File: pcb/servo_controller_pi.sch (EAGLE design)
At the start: 126 parts, among them IC1 PIC18F452, IC2 DS1307, IC3 MAX4173FESA+, IC4 LM2936MP-3.3, IC6 LM386M-1, IC7 GY-27, IC8 MCP23017SO, Q1 10Mhz, Q2 BC848ASMD, Q3 BC848ASMD

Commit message: BleuettePi encore !
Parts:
- removed D4, D5, D7: 5V1, diode:ZENER-DIODESOT23
- removed R19, R20, R21, R22: 10k, rcl:R-EU_M0805
- removed U$1: MCP3424-E/ST, eagleParts_MCP3424:MCP3424-E/ST
- added R30, R32, R34, R36: 10k 1%, rcl:R-EU_M0805
- added R31, R33, R35, R37: 6.8k 1%, rcl:R-EU_M0805
- added SV5: (no value), con-lstb:MA03-2
- added U$4: MCP3424-E/SL, eagleParts:MCP3424-E/SL
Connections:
- removed net MCP_LIPO_VOLTAGE: SJ1.3, U$1.CH3+
- new net CAN0: R30.1, R31.2, SV5.1, U$4.CH1+
- new net CAN1: R32.1, R33.2, SV5.2, U$4.CH2+
- new net CAN2: R34.1, R35.2, SV5.3, U$4.CH3+
- new net CAN3: R36.1, R37.2, SJ1.3, SV5.4, U$4.CH4+
- net +5V: now also R30.2, R32.2, R34.2, R36.2, SV5.6, U$4.VDD; no longer U$1.VDD
- net MCP_SERVO_CURRENT: no longer U$1.CH4+
- net SCL: now also U$4.SCL; no longer U$1.SCL
- net SDA: now also U$4.SDA; no longer U$1.SDA
- net VSS: now also R31.1, R33.1, R35.1, R37.1, SV5.5, U$4.ADR0, U$4.ADR1, U$4.CH1-, U$4.CH2-, U$4.CH3-, U$4.CH4-, U$4.VSS; no longer U$1.ADR0, U$1.ADR1, U$1.CH1-, U$1.CH2-, U$1.CH3-, U$1.CH4-, U$1.VSS
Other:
- moved on the sheet: C22, C24, DRDY1

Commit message: BleuettePi
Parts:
- removed I2C: (no value), con-lstb:MA04-1
- renumbered SJ1 to J_VOLT, SJ2 to J_CURRENT
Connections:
- removed net MCP_SERVO_CURRENT: J_CURRENT.3
- new net N$18: R30.1, R31.2, U$4.CH1+
- new net N$28: R32.1, R33.2, U$4.CH2+
- new net N$29: R34.1, R35.2, U$4.CH3+
- new net N$30: R36.1, R37.2, U$4.CH4+
- net +3V3: no longer I2C.4
- net +5V: no longer R30.2, R32.2, R34.2, R36.2
- net CAN0: now also R30.2; no longer R30.1, R31.2, U$4.CH1+
- net CAN1: now also R32.2; no longer R32.1, R33.2, U$4.CH2+
- net CAN2: now also J_CURRENT.3, R34.2; no longer R34.1, R35.2, U$4.CH3+
- net CAN3: now also R36.2; no longer R36.1, R37.2, U$4.CH4+
- net INTA: now also U$3.24-SPI-CE0-N; no longer U$3.22-GPIO6
- net INTB: now also U$3.26-SPI-CE1-N; no longer U$3.24-SPI-CE0-N
- net SCL: no longer I2C.3
- net SDA: no longer I2C.2
- net VSS: no longer I2C.1
- net __: now also U$3.22-GPIO6; no longer U$3.26-SPI-CE1-N

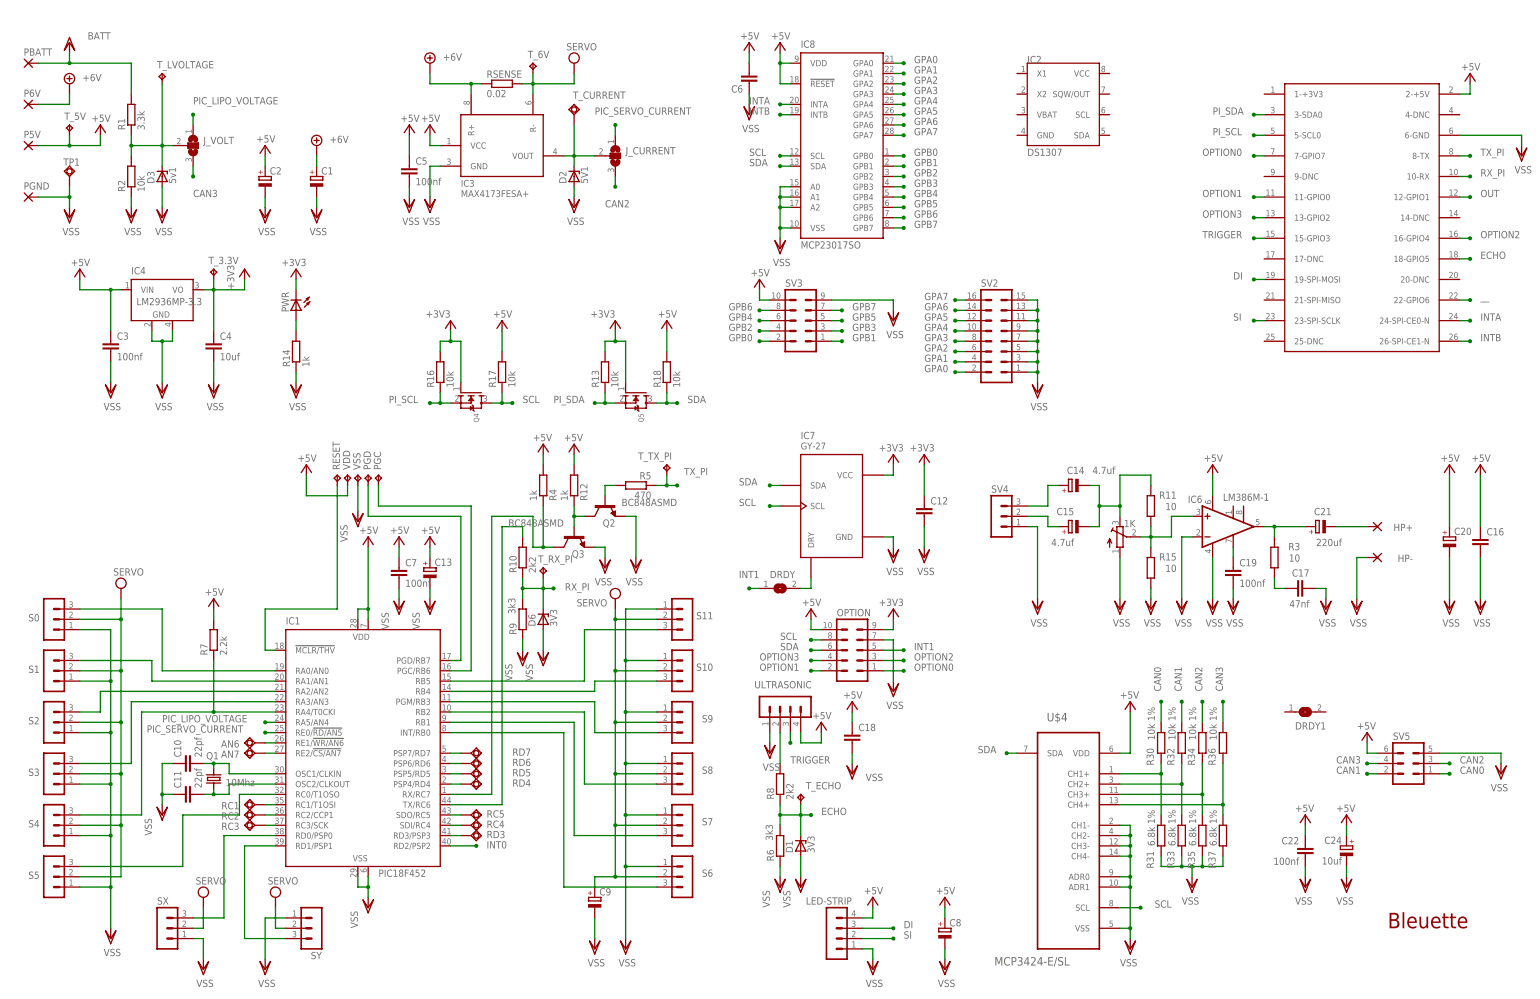
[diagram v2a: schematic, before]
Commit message: BleuettePi : Add RTC Clock
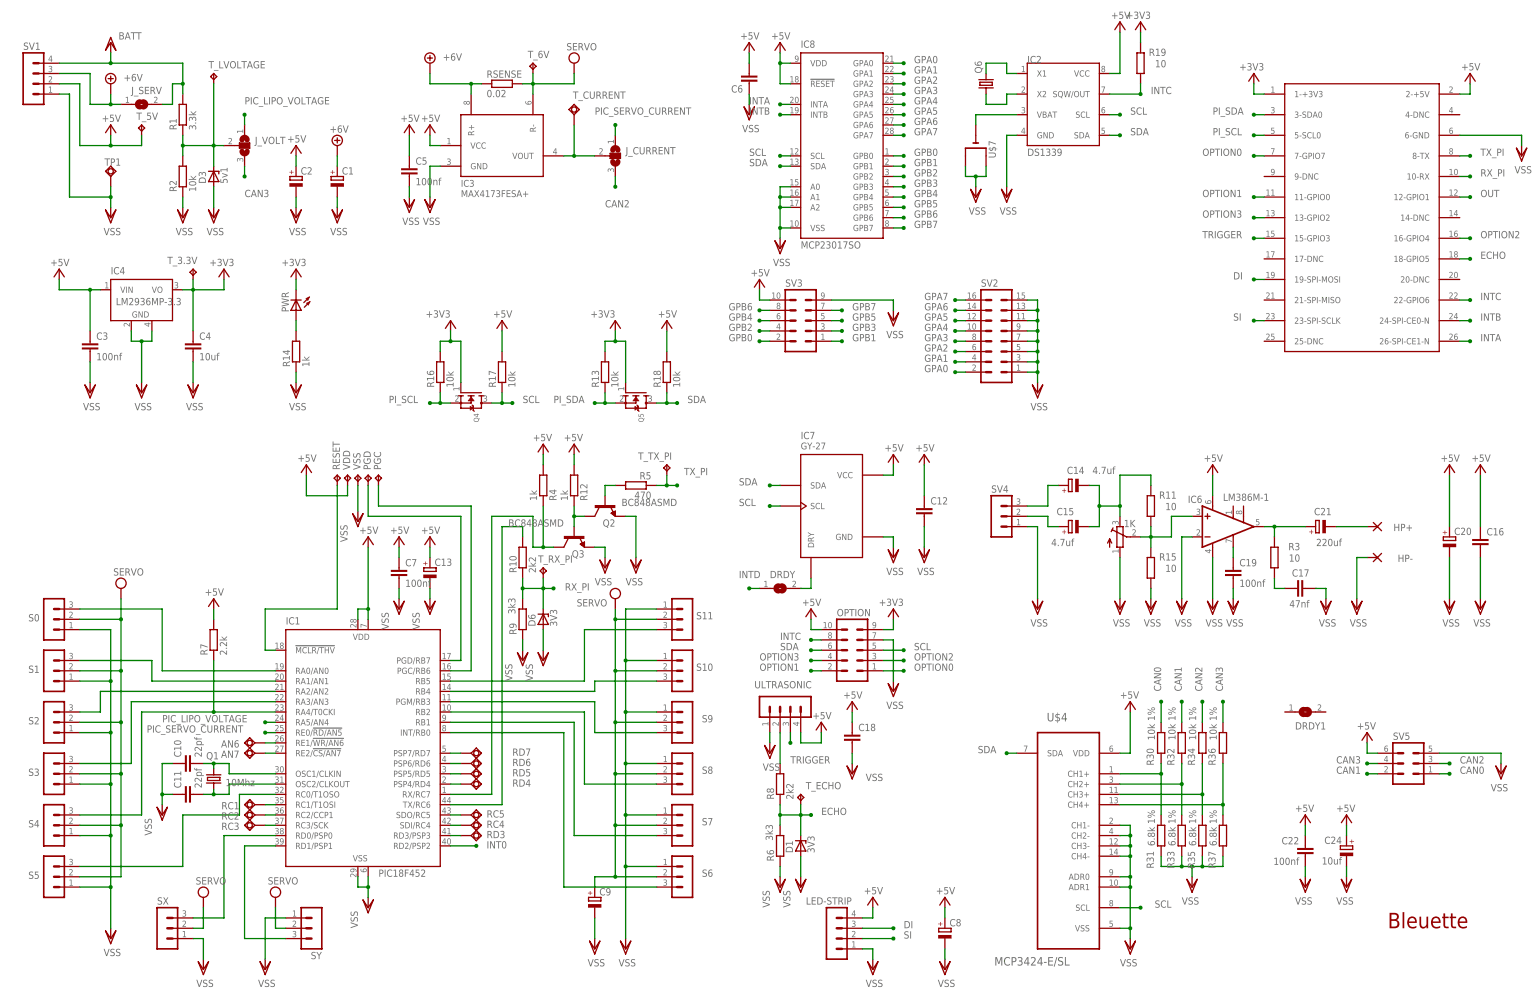
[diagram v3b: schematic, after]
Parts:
- removed D2: 5V1, diode:ZENER-DIODESOT23
- removed P5V, P6V, PBATT, PGND: (no value), wirepad:2,15/1,0
- added J_SERV: (no value), jumper:SJ
- added Q6: (no value), crystal:CRYSTALTC26H
- added R19: 10, rcl:R-EU_M0805
- added SV1: (no value), con-lstb:MA04-1
- added U$7: (no value), adafruit:CR1220SMT
- IC2: value DS1307 -> DS1339
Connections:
- removed net INT1: DRDY.1, OPTION.5
- removed net __: U$3.22-GPIO6
- new net INTC: IC2.SQW/OUT, OPTION.8, R19.1, U$3.22-GPIO6
- new net INTD: DRDY.1
- new net N$33: IC2.X1, Q6.2
- new net N$34: IC2.X2, Q6.1
- new net N$58: IC2.VBAT, U$7.-
- net +3V3: now also R19.2, U$3.1-+3V3; no longer C12.1, IC7.VCC
- net +5V: now also C12.1, IC2.VCC, IC7.VCC, SV1.2; no longer P5V.P
- net +7V: now also J_SERV.1, SV1.3; no longer P6V.P
- net INTA: now also U$3.26-SPI-CE1-N; no longer U$3.24-SPI-CE0-N
- net INTB: now also U$3.24-SPI-CE0-N; no longer U$3.26-SPI-CE1-N
- net SCL: now also IC2.SCL, OPTION.5; no longer OPTION.8
- net SDA: now also IC2.SDA
- net SERVO_CURRENT: no longer D2.C
- net VDD: now also J_SERV.2, SV1.4; no longer PBATT.P
- net VSS: now also IC2.GND, SV1.1, U$7.+, U$7.+1; no longer D2.A, PGND.P
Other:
- note added: "J_CURRENT : Servo current read by MCP or PIC"
- note added: "J_SERV : If servo power is same than battery"
- note added: "J_VOLT : Battery voltage read by MCP or PIC"
- moved on the sheet: C1, C2, C3, C4, D3, IC4, J_VOLT, R1, R2, TP1, T_3.3V, T_5V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

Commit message: BleuettePi
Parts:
- added C23, C25, C26, C27, C28, C29: 100nf, rcl:C-EUC0805
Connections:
- net N$18: now also C23.1
- net N$28: now also C25.1
- net N$29: now also C26.1
- net N$30: now also C27.1
- net PIC_LIPO_VOLTAGE: now also C29.1
- net PIC_SERVO_CURRENT: now also C28.1
- net VSS: now also C23.2, C25.2, C26.2, C27.2, C28.2, C29.2
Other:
- moved on the sheet: C10, C11, C22, C24, DRDY1, Q1, R30, R31, R32, R33, R34, R35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

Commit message: BleuettePi, modif ADC
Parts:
- removed AN6, AN7, RC4, RC5, RD3, RD4, RD5, RD6, RD7: TPSQTP06SQ, testpad:TPSQTP06SQ
- removed C28, C29: 100nf, rcl:C-EUC0805
- removed DRDY1: (no value), jumper:SJ
- removed J_CURRENT, J_VOLT: (no value), jumper:SJ2W
- removed R30, R32, R34, R36: 10k 1%, rcl:R-EU_M0805
- removed R31, R33, R35, R37: 6.8k 1%, rcl:R-EU_M0805
- removed R7: 2.2k, rcl:R-EU_M0805
- removed U$4: MCP3424-E/SL, eagleParts:MCP3424-E/SL
- C24: value 10uf -> 100nf; device rcl:CPOL-EUCT3528 -> rcl:C-EUC0805
- SV5: device con-lstb:MA03-2 -> con-lstb:MA04-2
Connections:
- net N$10 renamed SS6
- net N$11 renamed SS7
- net N$12 renamed SS8
- net N$13 renamed SS9
- net N$14 renamed SS10
- removed net CAN0: R30.2, SV5.1
- removed net CAN1: R32.2, SV5.2
- removed net CAN2: J_CURRENT.3, R34.2, SV5.3
- removed net CAN3: J_VOLT.3, R36.2, SV5.4
- removed net INT0: IC1.RD2/PSP2
- removed net LIPO_VOLTAGE: D3.C, J_VOLT.2, R1.1, R2.2, T_LVOLTAGE.TP
- removed net N$18: C23.1, R30.1, R31.2, U$4.CH1+
- removed net N$2: IC1.RA1/AN1, S1.3
- removed net N$20: AN7.TP, IC1.RE2/!CS/AN7
- removed net N$26: AN6.TP, IC1.RE1/!WR/AN6
- removed net N$28: C25.1, R32.1, R33.2, U$4.CH2+
- removed net N$29: C26.1, R34.1, R35.2, U$4.CH3+
- removed net N$3: IC1.RA2/AN2, S2.3
- removed net N$30: C27.1, R36.1, R37.2, U$4.CH4+
- removed net N$32: IC1.RB5, S11.3
- removed net N$4: IC1.RA3/AN3, S3.3
- removed net N$48: IC1.PSP7/RD7, RD7.TP
- removed net N$49: IC1.PSP6/RD6, RD6.TP
- removed net N$5: IC1.RA4/T0CKI, R7.1, S4.3
- removed net N$50: IC1.PSP5/RD5, RD5.TP
- removed net N$51: IC1.PSP4/RD4, RD4.TP
- removed net N$57: IC1.RD3/PSP3, RD3.TP
- removed net N$6: IC1.RC0/T1OSO, S5.3
- removed net PIC_LIPO_VOLTAGE: C29.1, IC1.RA5/AN4, J_VOLT.1
- removed net PIC_SERVO_CURRENT: C28.1, IC1.RE0/!RD/AN5, J_CURRENT.1
- removed net SERVO_CURRENT: IC3.VOUT, J_CURRENT.2, T_CURRENT.TP
- new net AN0: C27.2, IC1.RA0/AN0, SV5.1
- new net AN1: C26.2, IC1.RA1/AN1, SV5.2
- new net AN2: C25.2, IC1.RA2/AN2, SV5.3
- new net AN3: C24.2, IC1.RA3/AN3, SV5.4
- new net AN4: C23.2, IC1.RA5/AN4, SV5.5
- new net AN5: C22.2, IC1.RE0/!RD/AN5, SV5.6
- new net AN6: D3.C, IC1.RE1/!WR/AN6, R1.1, R2.2, T_LVOLTAGE.TP
- new net AN7: IC1.RE2/!CS/AN7, IC3.VOUT, T_CURRENT.TP
- new net SS0: IC1.RD2/PSP2, S0.3
- new net SS1: IC1.RD3/PSP3, S1.3
- new net SS11: IC1.RB5
- new net SS2: IC1.PSP4/RD4, S2.3
- new net SS3: IC1.PSP5/RD5, S3.3
- new net SS4: IC1.PSP6/RD6, S4.3
- new net SS5: IC1.PSP7/RD7, S5.3
- net +5V: now also SV5.8; no longer C22.1, C24.+, R7.2, SV5.6, U$4.VDD
- net INTD: now also IC1.RC0/T1OSO
- net N$1: now also S11.3; no longer IC1.RA0/AN0, S0.3
- net N$55: no longer RC4.TP
- net N$56: no longer RC5.TP
- net SCL: no longer U$4.SCL
- net SDA: no longer U$4.SDA
- net VSS: now also C22.1, C23.1, C24.1, C25.1, C26.1, C27.1, SV5.7; no longer C22.2, C23.2, C24.-, C25.2, C26.2, C27.2, C28.2, C29.2, R31.1, R33.1, R35.1, R37.1, SV5.5, U$4.ADR0, U$4.ADR1, U$4.CH1-, U$4.CH2-, U$4.CH3-, U$4.CH4-, U$4.VSS
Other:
- note added: "INTA : Interrupt from GPA port"
- note added: "INTB : Interrupt from GPB port"
- note added: "INTC : Interrupt from RTC Clock"
- note added: "INTD : Interrupt from PIC <- CONNECT ME !"
- note added: "Lier INT0 du PIC avec une entrée !"
- note removed: "ADC"
- note removed: "Bleuette"
- note removed: "Vérifier la taille de C24 qui doit être de 10uf / tantale"
- moved on the sheet: C22, C23, C25, C26, C27, C9

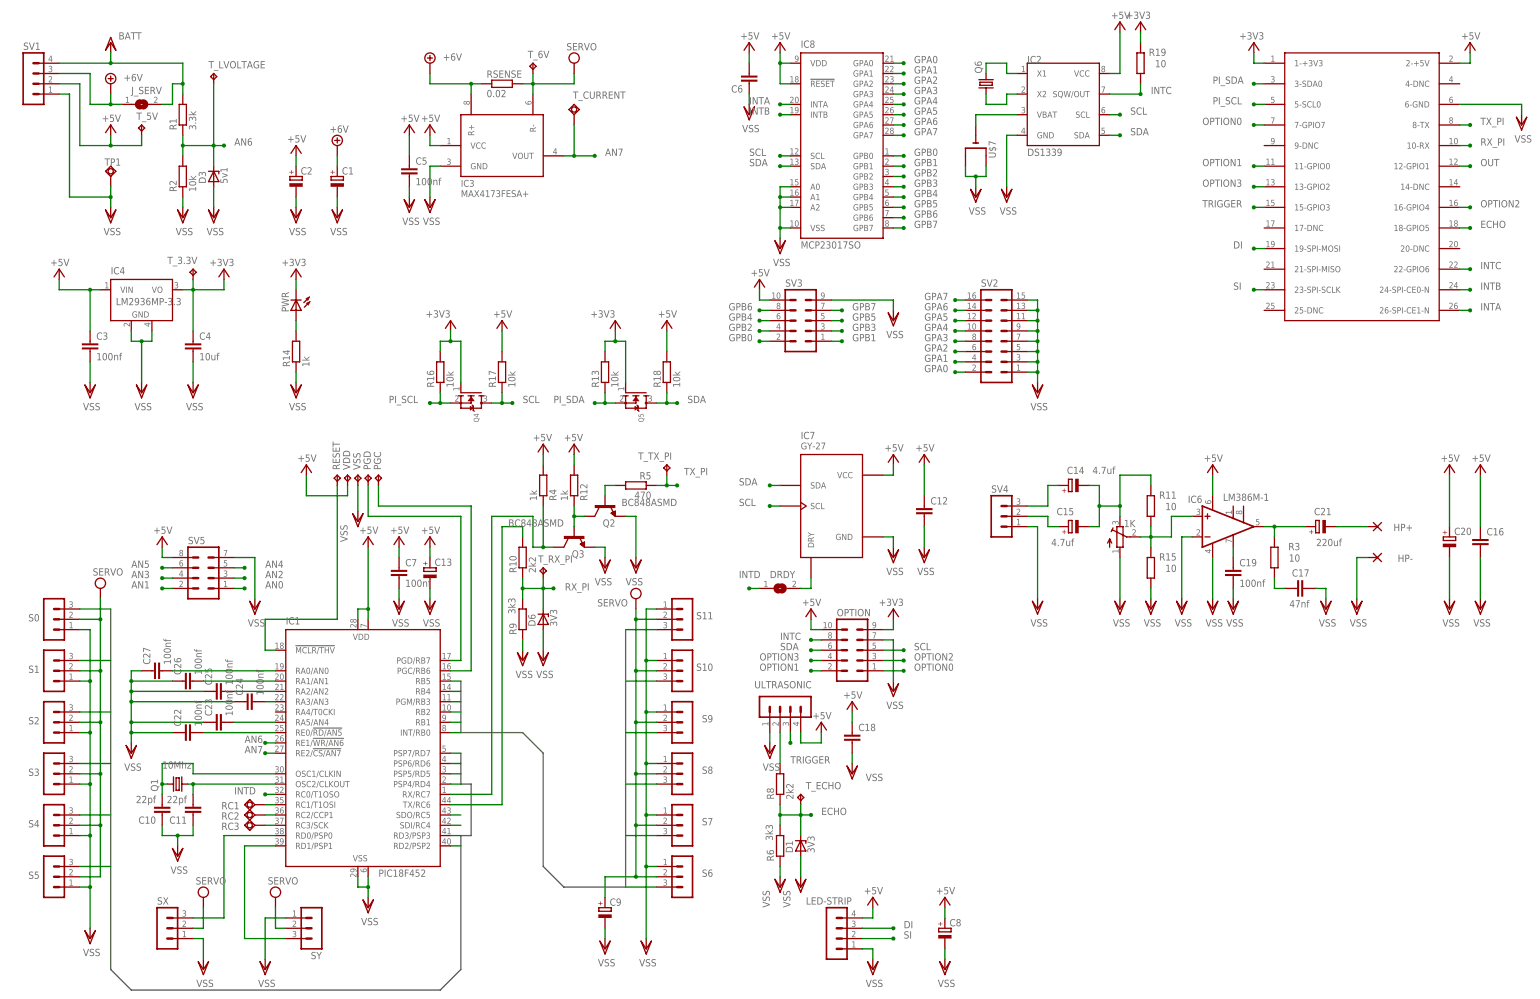
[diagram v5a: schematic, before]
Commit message: BleuettePi : ADC modif
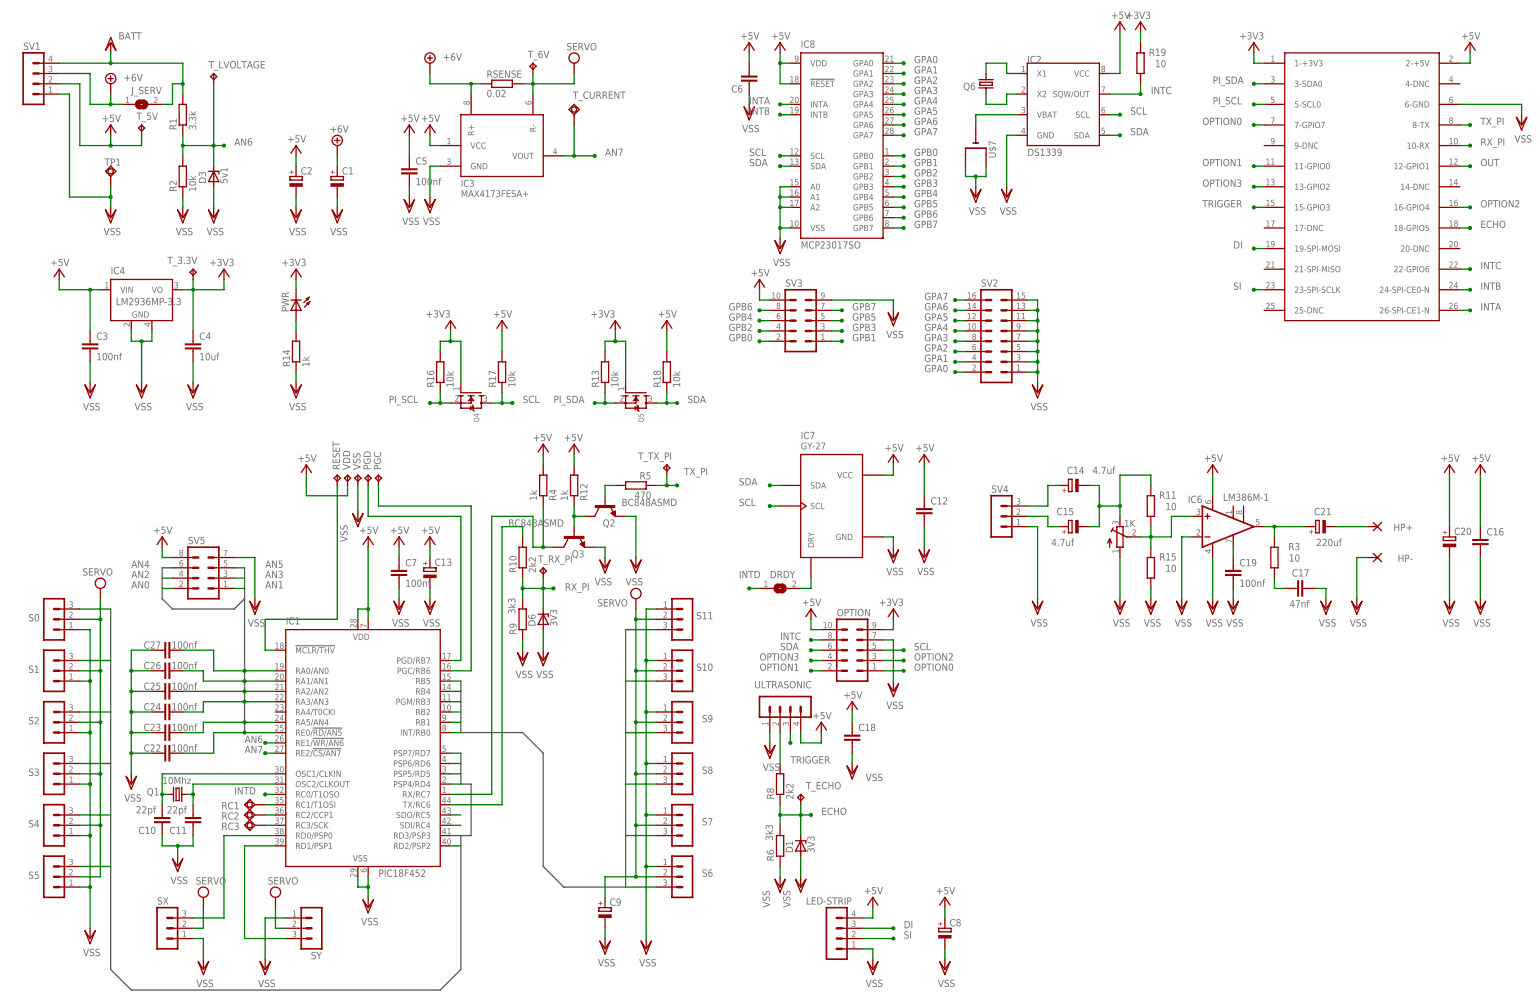
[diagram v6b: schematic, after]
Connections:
- net AN0: now also SV5.2; no longer SV5.1
- net AN1: now also SV5.1; no longer SV5.2
- net AN2: now also SV5.4; no longer SV5.3
- net AN3: now also SV5.3; no longer SV5.4
- net AN4: now also SV5.6; no longer SV5.5
- net AN5: now also SV5.5; no longer SV5.6
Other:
- moved on the sheet: C10, C11, C22, C23, C24, C25, C26, C27, Q1

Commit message: BleuettePi work !
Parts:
- removed D6: 3V3, diode:ZENER-DIODESOT23
- removed R5: 470, rcl:R-EU_M0805
- added C28, C29: 100nf, rcl:C-EUC0805
- Q2, Q3: value BC848ASMD -> (none); device transistor-npn:BC848ASMD -> adafruit:MOSFET-NREFLOW
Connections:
- removed net N$1: S11.3
- removed net N$21: Q2.C, Q3.B, R12.1
- removed net N$44: Q2.B, R5.2
- new net AGND: C22.1, C23.1, C24.1, C25.1, C26.1, C27.1, C28.1, C29.1, SV5.7
- net +3V3: now also Q2.G, Q3.G, R12.2, R9.2
- net +5V: now also R10.2; no longer R12.2
- net AN6: now also C28.2
- net AN7: now also C29.2
- net N$16: now also Q3.D, R10.1; no longer R10.2
- net N$33: now also Q6.1; no longer Q6.2
- net N$34: now also Q6.2; no longer Q6.1
- net RX_PI: now also Q3.S, R9.1; no longer D6.C, R10.1, R9.2
- net RX_PIC: now also Q2.D; no longer Q3.C
- net SS11: now also S11.3
- net TX_PI: now also Q2.S, R12.1; no longer R5.1
- net VSS: no longer C22.1, C23.1, C24.1, C25.1, C26.1, C27.1, D6.A, Q2.E, Q3.E, R9.1, SV5.7
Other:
- note added: "I2C level adapter"
- note removed: "J_CURRENT : Servo current read by MCP or PIC"
- note removed: "Level adapter"
- moved on the sheet: C22, C23, C24, C25, C26, C27, Q6, R10, R12, R4, R9, SV5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
